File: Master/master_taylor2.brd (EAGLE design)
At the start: 54.1 x 51.3 mm, 51 parts, among them J1 ISP, U1 ATMEGA128RFA1, U2 TPS73633-DBVT, U3 ULN2003ADR, Y1 16MHz

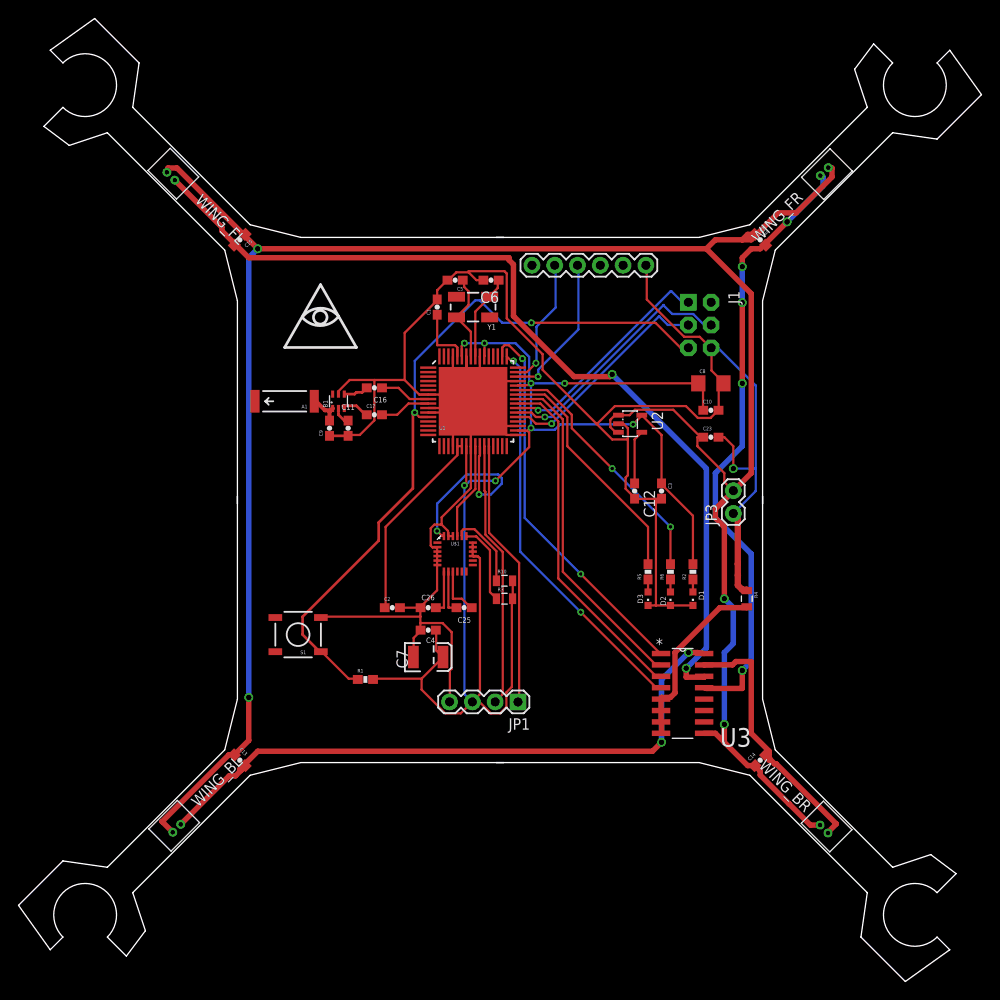
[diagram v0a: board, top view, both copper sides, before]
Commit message: Sparkfun's electrolytic footprint seemed sketchy so I switched to microbuilder
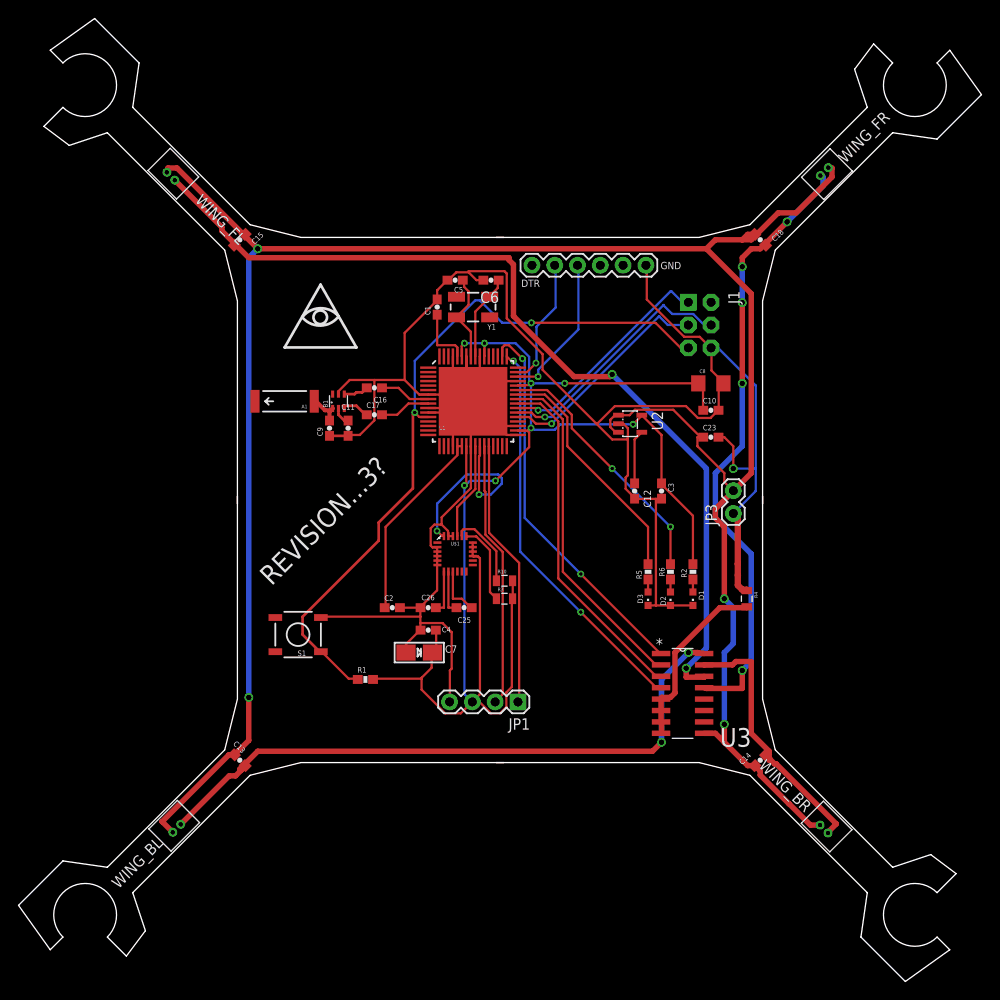
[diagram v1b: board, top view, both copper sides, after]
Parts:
- C7: device SparkFun-Capacitors:EIA3528 -> microbuilder:EIA3216-18/A-W
- moved C7 1.12 mm to (-9.00, -17.0)
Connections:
- net 3.3V: now also C7.+; no longer C7.A
- net GND: now also C7.-; no longer C7.C
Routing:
- net 3.3V: track 174.7 -> 174.1 mm
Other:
- board text added: "DTR"
- board text added: "GND"
- board text added: "REVISION...3?"
